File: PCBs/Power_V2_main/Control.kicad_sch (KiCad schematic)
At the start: 15 parts, among them J7 TYPE-C-31-M-12, J9 Conn_01x02, U1 ESP32-S3-WROOM-2, U6 USBLC6-4SC6

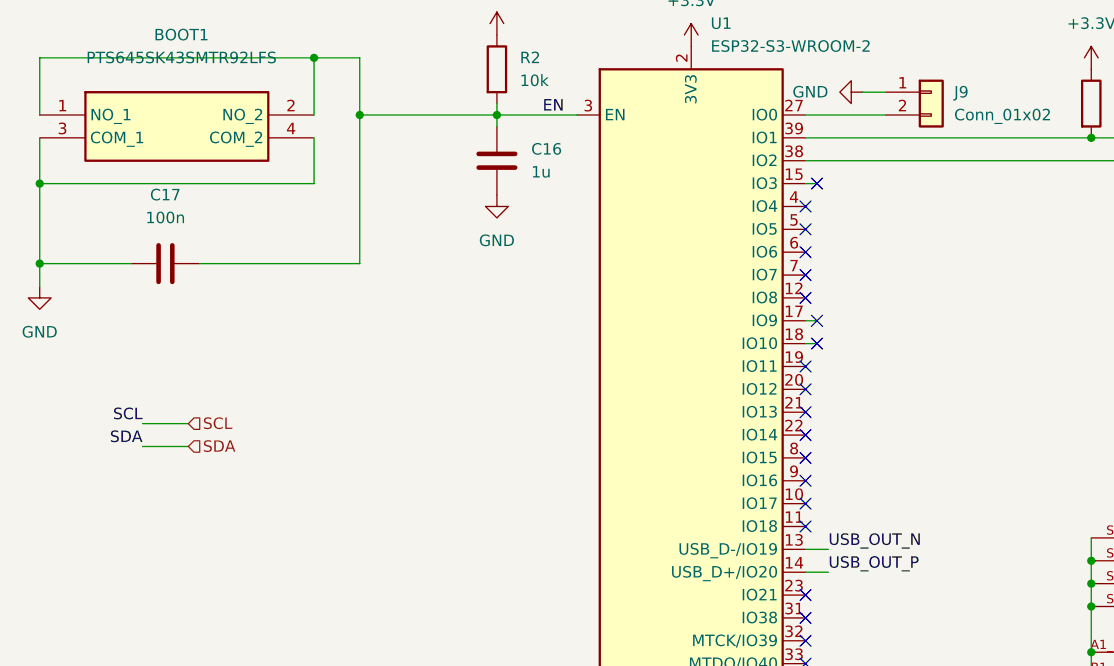
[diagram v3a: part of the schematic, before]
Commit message: added LED indicators to board and redid power distribution in PCIe
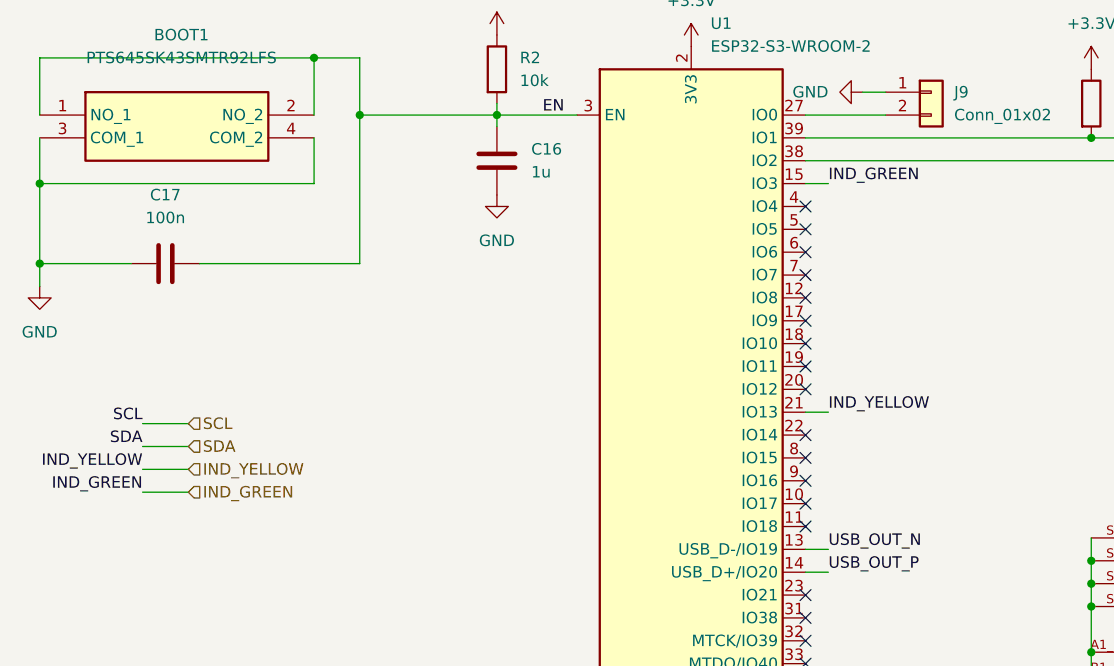
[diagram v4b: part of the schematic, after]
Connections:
- net IND_GREEN: now reaches U1.15 (IO3)
- net IND_YELLOW: now reaches U1.21 (IO13)
- no-connect marks 31 -> 29
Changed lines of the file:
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@@
+	)
+	(no_connect
+		(at 114.3 66.04)
+	)
+	(no_connect
+		(at 114.3 132.08)
+	)
+	(no_connect
+		(at 114.3 111.76)
+	)
+	(no_connect
+		(at 114.3 119.38)
+	)
+	(no_connect
+		(at 210.82 100.33)
 	)
 	(no_connect
@@
 	)
 	(no_connect
-		(at 114.3 66.04)
-	)
-	(no_connect
-		(at 114.3 132.08)
-	)
-	(no_connect
-		(at 114.3 111.76)
-	)
-	(no_connect
-		(at 114.3 119.38)
-	)
-	(no_connect
-		(at 210.82 100.33)
-	)
-	(no_connect
 		(at 114.3 91.44)
 	)
@@
 	)
 	(no_connect
-		(at 115.57 58.42)
+		(at 114.3 104.14)
 	)
 	(no_connect
@@
 	)
 	(no_connect
-		(at 114.3 83.82)
-	)
-	(no_connect
 		(at 114.3 68.58)
 	)
 	(no_connect
+		(at 114.3 73.66)
+	)
+	(no_connect
 		(at 114.3 124.46)
 	)
@@
 	)
 	(no_connect
-		(at 114.3 104.14)
-	)
-	(no_connect
 		(at 114.3 63.5)
 	)
 	(no_connect
+		(at 114.3 129.54)
+	)
+	(no_connect
 		(at 114.3 121.92)
 	)
@@
 	)
 	(no_connect
+		(at 114.3 127)
+	)
+	(no_connect
 		(at 114.3 116.84)
 	)
@@
 	)
 	(no_connect
-		(at 114.3 127)
-	)
-	(no_connect
 		(at 176.53 110.49)
 	)
 	(no_connect
-		(at 115.57 76.2)
-	)
-	(no_connect
-		(at 114.3 129.54)
-	)
-	(no_connect
-		(at 115.57 73.66)
+		(at 114.3 76.2)
 	)
 	(no_connect
@@
 	(wire
 		(pts
+			(xy 45.72 92.71) (xy 40.64 92.71)
+		)
+		(stroke
+			(width 0)
+			(type default)
+		)
+	)
+	(wire
+		(pts
 			(xy 80.01 49.53) (xy 80.01 50.8)
 		)
@@
 	(wire
 		(pts
+			(xy 45.72 90.17) (xy 40.64 90.17)
+		)
+		(stroke
+			(width 0)
+			(type default)
+		)
+	)
+	(wire
+		(pts
 			(xy 146.05 110.49) (xy 146.05 113.03)
 		)
@@
 	(wire
 		(pts
-			(xy 114.3 58.42) (xy 115.57 58.42)
-		)
-		(stroke
-			(width 0)
-			(type default)
-		)
-	)
-	(wire
-		(pts
 			(xy 80.01 50.8) (xy 88.9 50.8)
 		)
@@
 	(wire
 		(pts
-			(xy 114.3 76.2) (xy 115.57 76.2)
-		)
-		(stroke
-			(width 0)
-			(type default)
-		)
-	)
-	(wire
-		(pts
 			(xy 114.3 50.8) (xy 123.19 50.8)
 		)
@@
 	(wire
 		(pts
+			(xy 114.3 58.42) (xy 116.84 58.42)
+		)
+		(stroke
+			(width 0)
+			(type default)
+		)
+	)
+	(wire
+		(pts
 			(xy 29.21 69.85) (xy 29.21 67.31)
 		)
@@
 	(wire
 		(pts
+			(xy 114.3 83.82) (xy 116.84 83.82)
+		)
+		(stroke
+			(width 0)
+			(type default)
+		)
+	)
+	(wire
+		(pts
 			(xy 193.04 91.44) (xy 191.77 91.44)
 		)
@@
 	(wire
 		(pts
-			(xy 114.3 73.66) (xy 115.57 73.66)
-		)
-		(stroke
-			(width 0)
-			(type default)
-		)
-	)
-	(wire
-		(pts
 			(xy 123.19 48.26) (xy 120.65 48.26)
 		)
@@
 			(width 0)
 			(type default)
+		)
+	)
+	(label "IND_GREEN"
+		(at 40.64 92.71 180)
+		(effects
+			(font
+				(size 1.27 1.27)
+			)
+			(justify right bottom)
+		)
+	)
+	(label "IND_YELLOW"
+		(at 40.64 90.17 180)
+		(effects
+			(font
+				(size 1.27 1.27)
+			)
+			(justify right bottom)
+		)
+	)
+	(label "IND_GREEN"
+		(at 116.84 58.42 0)
+		(effects
+			(font
+				(size 1.27 1.27)
+			)
+			(justify left bottom)
 		)
 	)
@@
 		)
 	)
+	(label "IND_YELLOW"
+		(at 116.84 83.82 0)
+		(effects
+			(font
+				(size 1.27 1.27)
+			)
+			(justify left bottom)
+		)
+	)
 	(label "SCL"
 		(at 152.4 53.34 0)
@@
 		)
 	)
+	(hierarchical_label "IND_GREEN"
+		(shape input)
+		(at 45.72 92.71 0)
+		(effects
+			(font
+				(size 1.27 1.27)
+			)
+			(justify left)
+		)
+	)
+	(hierarchical_label "IND_YELLOW"
+		(shape input)
+		(at 45.72 90.17 0)
+		(effects
+			(font
+				(size 1.27 1.27)
+			)
+			(justify left)
+		)
+	)

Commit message: modification to LED switches
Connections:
- net IND_GREEN: now also U1.21 (IO13); no longer U1.15 (IO3)
- net IND_YELLOW: now also U1.15 (IO3); no longer U1.21 (IO13)
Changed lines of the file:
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@@
-		)
-	)
-	(label "IND_GREEN"
-		(at 116.84 58.42 0)
-		(effects
-			(font
-				(size 1.27 1.27)
-			)
-			(justify left bottom)
 		)
 	)
@@
 			)
 			(justify right bottom)
+		)
+	)
+	(label "IND_GREEN"
+		(at 116.84 83.82 0)
+		(effects
+			(font
+				(size 1.27 1.27)
+			)
+			(justify left bottom)
 		)
 	)
@@
 	)
 	(label "IND_YELLOW"
-		(at 116.84 83.82 0)
+		(at 116.84 58.42 0)
 		(effects
 			(font

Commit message: Changes from meeting
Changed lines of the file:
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@@
 		(dnp no)
 		(property "Reference" "BOOT1"
-			(at 44.958 41.91 0)
+			(at 44.45 39.37 0)
 			(effects
 				(font
@@
 		)
 		(property "Value" "PTS645SK43SMTR92LFS"
-			(at 44.958 44.45 0)
+			(at 44.45 41.91 0)
 			(effects
 				(font

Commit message: follow up changes from meeting
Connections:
- net IND_YELLOW: now also U1.18 (IO10); no longer U1.15 (IO3)
- new net IND_SIREN: U1.15 (IO3)
- no-connect marks 29 -> 28
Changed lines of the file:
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@@
+	)
+	(no_connect
+		(at 114.3 73.66)
 	)
 	(no_connect
@@
 	)
 	(no_connect
-		(at 114.3 73.66)
-	)
-	(no_connect
 		(at 114.3 124.46)
 	)
@@
 	)
 	(no_connect
-		(at 114.3 76.2)
-	)
-	(no_connect
 		(at 176.53 113.03)
 	)
@@
 	(wire
 		(pts
+			(xy 45.72 95.25) (xy 40.64 95.25)
+		)
+		(stroke
+			(width 0)
+			(type default)
+		)
+	)
+	(wire
+		(pts
 			(xy 29.21 44.45) (xy 59.69 44.45)
 		)
@@
 		(pts
 			(xy 248.92 22.86) (xy 243.84 22.86)
+		)
+		(stroke
+			(width 0)
+			(type default)
+		)
+	)
+	(wire
+		(pts
+			(xy 114.3 76.2) (xy 116.84 76.2)
 		)
 		(stroke
@@
 		)
 	)
+	(label "IND_SIREN"
+		(at 40.64 95.25 180)
+		(effects
+			(font
+				(size 1.27 1.27)
+			)
+			(justify right bottom)
+		)
+	)
 	(label "USB_OUT_P"
 		(at 116.84 101.6 0)
@@
 		)
 	)
-	(label "IND_YELLOW"
-		(at 116.84 58.42 0)
-		(effects
-			(font
-				(size 1.27 1.27)
-			)
-			(justify left bottom)
-		)
-	)
 	(label "SCL"
 		(at 152.4 53.34 0)
@@
 		)
 	)
+	(label "IND_SIREN"
+		(at 116.84 58.42 0)
+		(effects
+			(font
+				(size 1.27 1.27)
+			)
+			(justify left bottom)
+		)
+	)
 	(label "USB_OUT_N"
 		(at 203.2 97.79 180)
@@
 			)
 			(justify right bottom)
+		)
+	)
+	(label "IND_YELLOW"
+		(at 116.84 76.2 0)
+		(effects
+			(font
+				(size 1.27 1.27)
+			)
+			(justify left bottom)
 		)
 	)
@@
 		(effects
 			(font
+				(size 1.27 1.27)
+			)
+			(justify left)
+		)
+	)
+	(hierarchical_label "IND_SIREN"
+		(shape input)
+		(at 45.72 95.25 0)
+		(effects
+			(font
